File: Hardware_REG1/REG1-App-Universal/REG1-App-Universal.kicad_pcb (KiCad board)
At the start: 2 copper layers, 83 x 32.8 mm, 31 parts, among them J1 REG1_App_Connector, J2 Conn_01x10, Q1 BC857C,215, Q2 STN93003, Q3 STN1HNK60, Q4 BSS123, U1 EL357N(C)(TA)-G, U2 EL357N(C)(TA)-G, U3 DB125-3.81-2P

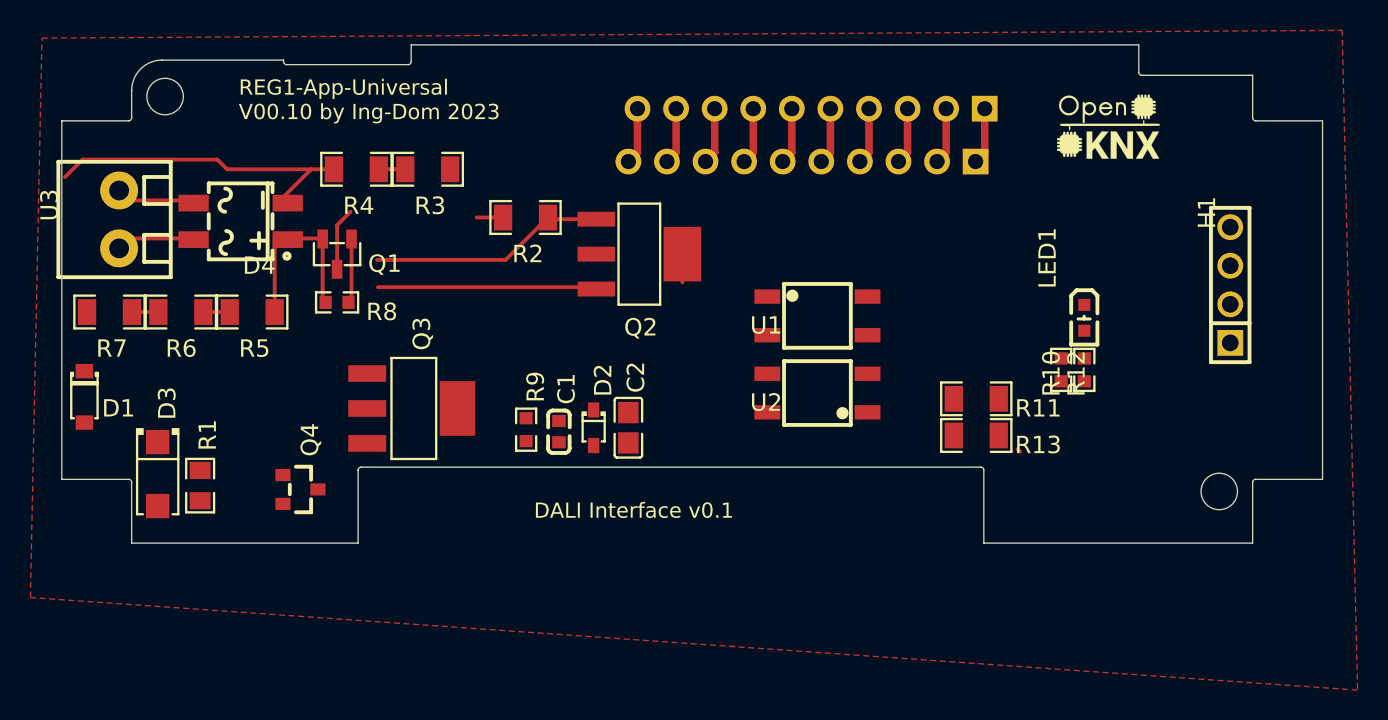
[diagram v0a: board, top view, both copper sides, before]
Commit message: added DALI lib
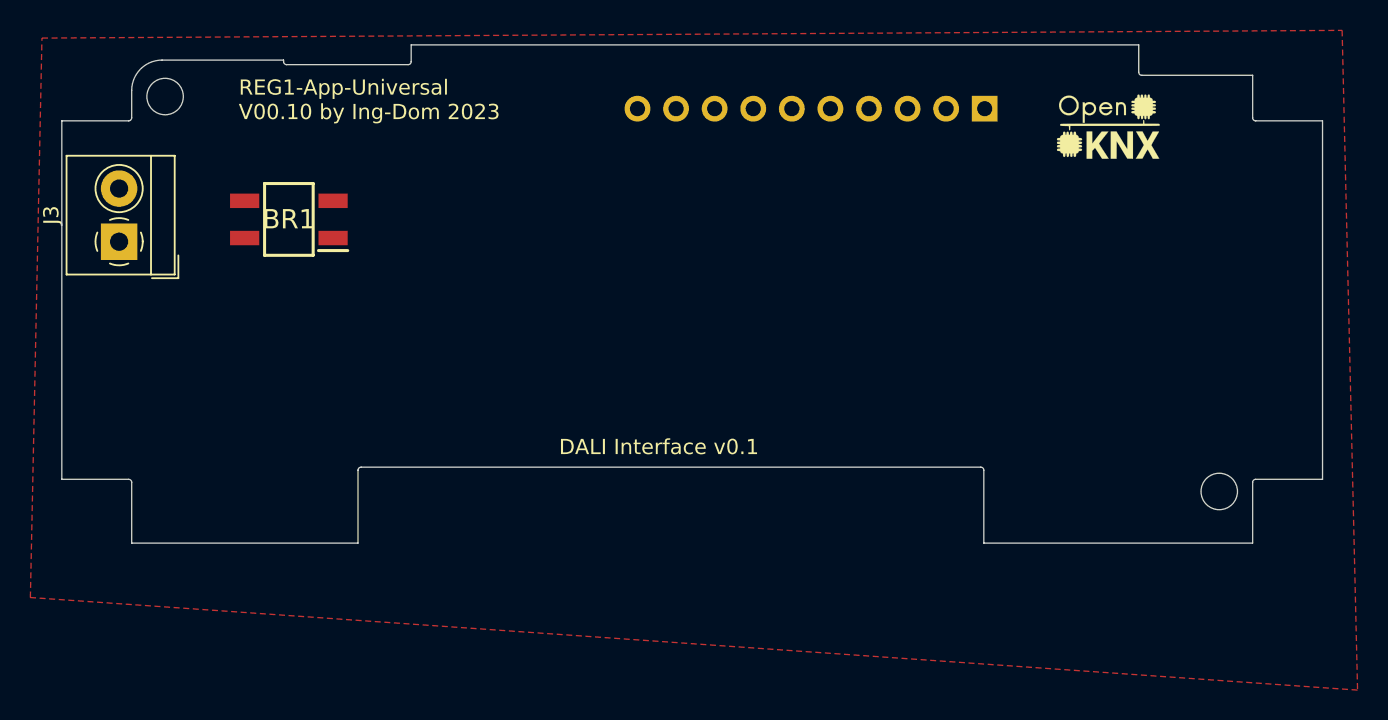
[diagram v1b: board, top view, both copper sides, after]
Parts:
- removed C1: 1nF, easyeda:C0603
- removed C2: 2.2uF, easyeda:C0805
- removed D1: MMSZ4711T1G, easyeda:SOD-123_L2.8-W1.8-LS3.7-RD
- removed D2: UDZSTE-175.6B, easyeda:SOD-323_L1.8-W1.3-LS2.5-RD
- removed D3: 1SMA4746, easyeda:SMA_L4.4-W2.5-LS5.2-R-RD
- removed D4: MB10S_C2488, easyeda:MBS_L4.7-W3.8-P2.40-LS7.0-TL
- removed H1: 210-91-04GB01, easyeda:HDR-TH_4P-P2.54-V-M
- removed J2: Conn_01x10, Connector_PinHeader_2.54mm:PinHeader_1x10_P2.54mm_Vertical
- removed LED1: 0603White light_C2290, easyeda:LED0603-R-RD_WHITE
- removed Q1: BC857C,215, easyeda:SOT-23-3_L2.9-W1.3-P1.90-LS2.4-BR
- removed Q2: STN93003, easyeda:SOT-223-4_L6.5-W3.5-P2.30-LS7.0-BR
- removed Q3: STN1HNK60, easyeda:SOT-223-3_L6.5-W3.4-P2.30-LS7.0-BR
- removed Q4: BSS123, easyeda:SOT-23_L2.9-W1.3-P1.90-LS2.4-BR
- removed R1: 16kΩ, easyeda:R0805
- removed R10, R12, R9: 4.7kΩ, easyeda:R0603
- removed R11: 1kΩ, easyeda:R1206
- removed R13: 300Ω, easyeda:R1206
- removed R2, R3, R4, R5, R6, R7: 68kΩ, easyeda:R1206
- removed R8: 390Ω, easyeda:R0603
- removed U1, U2: EL357N(C)(TA)-G, easyeda:OPTO-SMD-4_L4.4-W4.1-P2.54-LS7.0-TL
- removed U3: DB125-3.81-2P, easyeda:CONN-TH_2P-P3.81_L7.4-W7.6
- added BR1: MB10S, DALI:SOP245P670X290-4N, F.Cu at (84.9, 101.6)
- added J3: DALI, TerminalBlock_4Ucon:TerminalBlock_4Ucon_1x02_P3.50mm_Horizontal, F.Cu at (73.8, 103.1)
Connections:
- J1 pad 1: Net-(J1-Pad1) -> unconnected-(J1-GP16-Pad1)
- J1 pad 10: Net-(J1-Pad10) -> unconnected-(J1-VCC2-Pad10)
- J1 pad 2: Net-(J1-Pad2) -> unconnected-(J1-GP17-Pad2)
- J1 pad 3: Net-(J1-Pad3) -> unconnected-(J1-GP18-Pad3)
- J1 pad 4: Net-(J1-Pad4) -> unconnected-(J1-GP26-Pad4)
- J1 pad 5: Net-(J1-Pad5) -> unconnected-(J1-GP27-Pad5)
- J1 pad 6: Net-(J1-Pad6) -> unconnected-(J1-GP28-Pad6)
- J1 pad 7: Net-(J1-Pad7) -> unconnected-(J1-GP29-Pad7)
- J1 pad 8: Net-(J1-Pad8) -> unconnected-(J1-GND-Pad8)
- J1 pad 9: Net-(J1-Pad9) -> unconnected-(J1-3V3-Pad9)
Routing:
- net DALI-: track 21.3 -> 0.00 mm
- net Q1_3: track 19.8 -> 0.00 mm
- net Q1_1: track 18.7 -> 0.00 mm
- net DALI+: track 12.4 -> 0.00 mm
- net U3_2: track 4.66 -> 0.00 mm
- net U3_1: track 4.66 -> 0.00 mm
- net Net-(J1-Pad8): track 3.73 -> 0.00 mm
- net Net-(J1-Pad6): track 3.73 -> 0.00 mm
- net Net-(J1-Pad3): track 3.73 -> 0.00 mm
- net Net-(J1-Pad10): track 3.73 -> 0.00 mm
- net Net-(J1-Pad9): track 3.73 -> 0.00 mm
- net Net-(J1-Pad7): track 3.73 -> 0.00 mm
- net Net-(J1-Pad5): track 3.73 -> 0.00 mm
- net Net-(J1-Pad4): track 3.73 -> 0.00 mm
- net Net-(J1-Pad2): track 3.73 -> 0.00 mm
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- added copper zone on F.Cu, net (none)
- removed copper zone on F.Cu, net GND

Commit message: updated pcb
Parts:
- added C1: 1n, Capacitor_SMD:C_0603_1608Metric, F.Cu at (122.5, 113.3)
- added C2: 2.2u, Capacitor_SMD:C_0805_2012Metric, F.Cu at (128.1, 113.0)
- added D1: 1SMA4746, DALI:DIOM4325X250N, F.Cu at (93.8, 111.1)
- added D2: D_Zener_Small, Diode_SMD:D_SOD-123, F.Cu at (90.0, 110.7)
- added D3: UDZSTE-175.6B, DALI:SODFL2512X90N, F.Cu at (125.3, 113.0)
- added D4: LED, LED_SMD:LED_0603_1608Metric, F.Cu at (145.9, 102.4)
- added Q1: BSS123, DALI:SOT23, F.Cu at (104.3, 112.2)
- added Q2: BC857, Package_TO_SOT_SMD:SOT-23, F.Cu at (102.0, 101.8)
- added R1: 100k, Resistor_SMD:R_1206_3216Metric, F.Cu at (91.6, 98.3)
- added R10: 1k, Resistor_SMD:R_1206_3216Metric, F.Cu at (143.6, 110.5)
- added R11: 300, Resistor_SMD:R_1206_3216Metric, F.Cu at (148.4, 110.5)
- added R2: 100k, Resistor_SMD:R_1206_3216Metric, F.Cu at (96.4, 98.3)
- added R3: 390, Resistor_SMD:R_0603_1608Metric, F.Cu at (101.9, 104.6)
- added R4: 100k, Resistor_SMD:R_1206_3216Metric, F.Cu at (83.7, 110.7)
- added R5: 100k, Resistor_SMD:R_1206_3216Metric, F.Cu at (86.7, 110.7)
- added R6: 16k, Resistor_SMD:R_0805_2012Metric, F.Cu at (99.9, 112.3)
- added R7: 4.7k, Resistor_SMD:R_0603_1608Metric, F.Cu at (120.0, 113.3)
- added R8: 4.7k, Resistor_SMD:R_0603_1608Metric, F.Cu at (142.6, 102.4)
- added R9: 4.7k, Resistor_SMD:R_0603_1608Metric, F.Cu at (144.5, 104.1)
- added U1: EL357N(A)(TA)-G, DALI:SOP254P700X200-4N, F.Cu at (136.0, 103.6)
- added U2: EL357N(A)(TA)-G, DALI:SOP254P700X200-4N, F.Cu at (136.0, 109.5)
- added U3: STN93003, DALI:SOT230P700X180-4N, F.Cu at (113.9, 102.1)
- added U4: STN1HNK60, DALI:SOT-223, F.Cu at (113.9, 111.0)
- moved BR1 2.30 mm to (82.7, 101.3)
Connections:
- BR1 pad 1: unconnected-(BR1-+-Pad1) -> Dali+
- BR1 pad 2: unconnected-(BR1---Pad2) -> DALI-
- J1 pad 1: unconnected-(J1-GP16-Pad1) -> /D_RX
- J1 pad 2: unconnected-(J1-GP17-Pad2) -> /D_TX
- J1 pad 8: unconnected-(J1-GND-Pad8) -> GND
- J1 pad 9: unconnected-(J1-3V3-Pad9) -> +3.3V
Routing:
- net DALI-: track 0.00 -> 68.3 mm
- net Dali+: track 0.00 -> 50.3 mm, vias 0 -> 2
- net +3.3V: track 0.00 -> 42.8 mm, vias 0 -> 1
- net /D_TX: track 0.00 -> 34.4 mm
- net Net-(C1-Pad1): track 0.00 -> 34.0 mm
- net Net-(U1-Pad1): track 0.00 -> 22.3 mm
- net Net-(Q2-C): track 0.00 -> 17.3 mm
- net /D_RX: track 0.00 -> 17.0 mm
- net Net-(C2-Pad1): track 0.00 -> 15.1 mm
- net Net-(D2-A): track 0.00 -> 14.3 mm
- net Net-(Q2-B): track 0.00 -> 12.0 mm
- net Net-(BR1-~_1): track 0.00 -> 6.21 mm
- net Net-(BR1-~_2): track 0.00 -> 6.18 mm
- net Net-(D2-K): track 0.00 -> 3.38 mm
- net Net-(R10-Pad1): track 0.00 -> 3.22 mm
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- added copper zone on F.Cu, net GND
- removed copper zone on F.Cu, net (none)
